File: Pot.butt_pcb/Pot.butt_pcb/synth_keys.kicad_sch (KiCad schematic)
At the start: 60 parts, among them SW11 Cherry_MX_1u, SW12 Cherry_MX_1u, SW13 Cherry_MX_1u, SW14 Cherry_MX_1u, SW15 Cherry_MX_1u, SW16 Cherry_MX_1u, SW17 Cherry_MX_1u, SW18 Cherry_MX_1u, SW19 Cherry_MX_1u, SW20 Cherry_MX_1u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

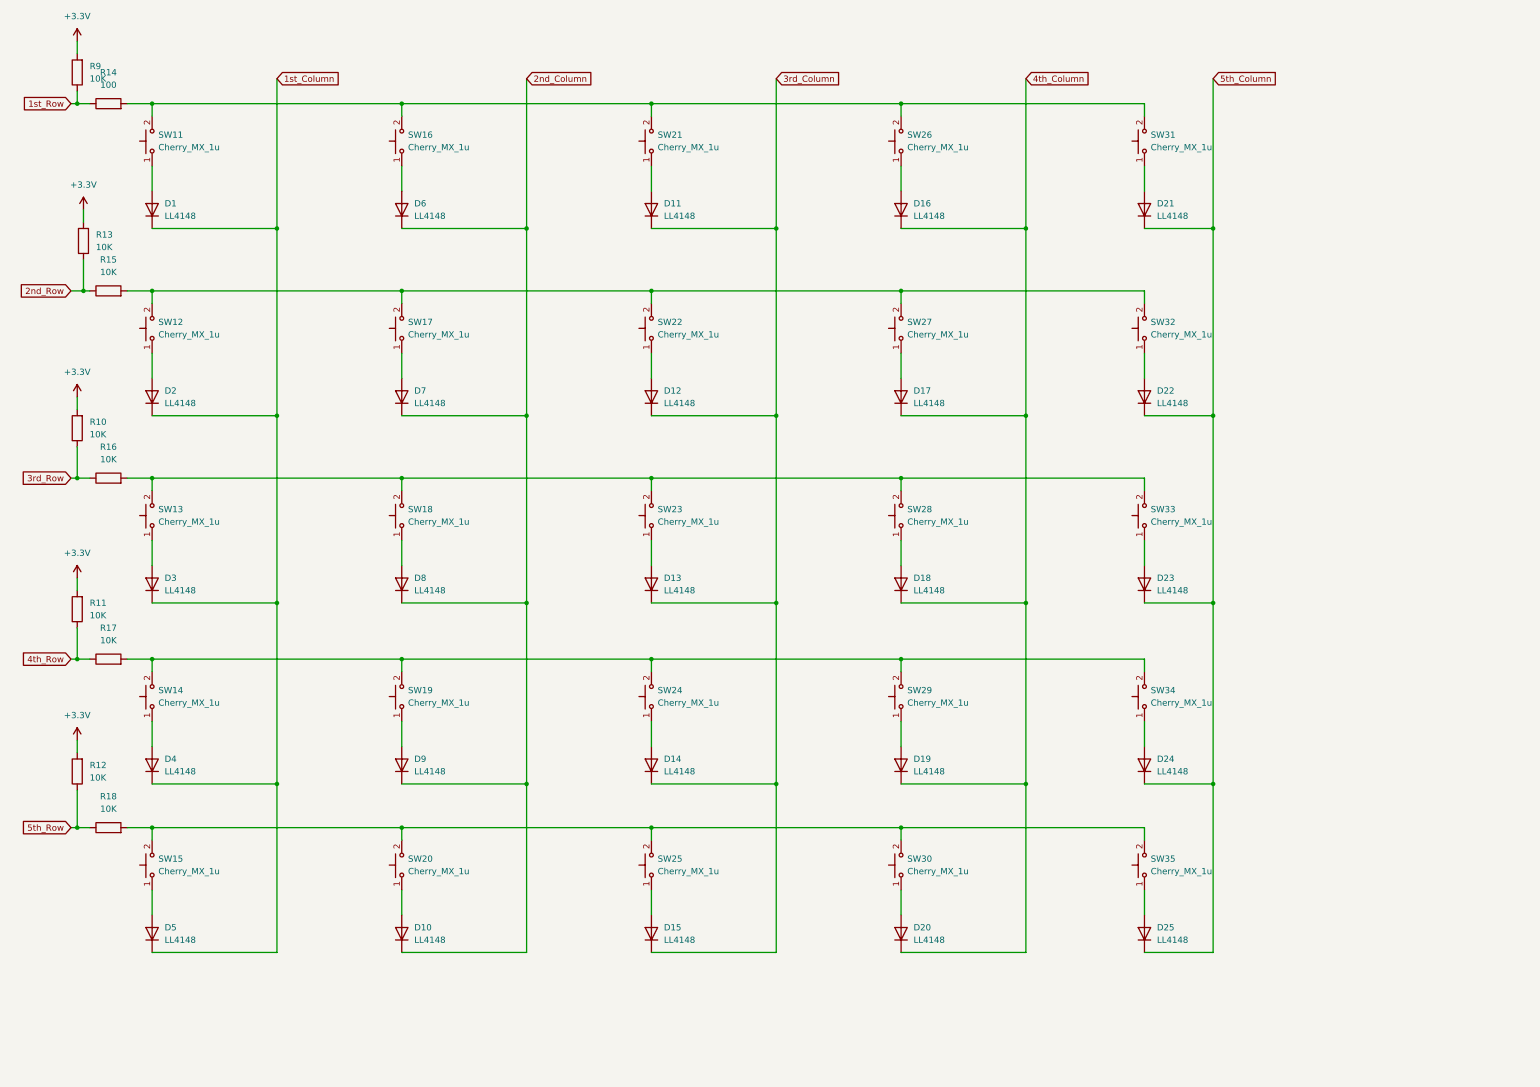
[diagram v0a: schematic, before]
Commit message: fixing keyboard and pot project schematics
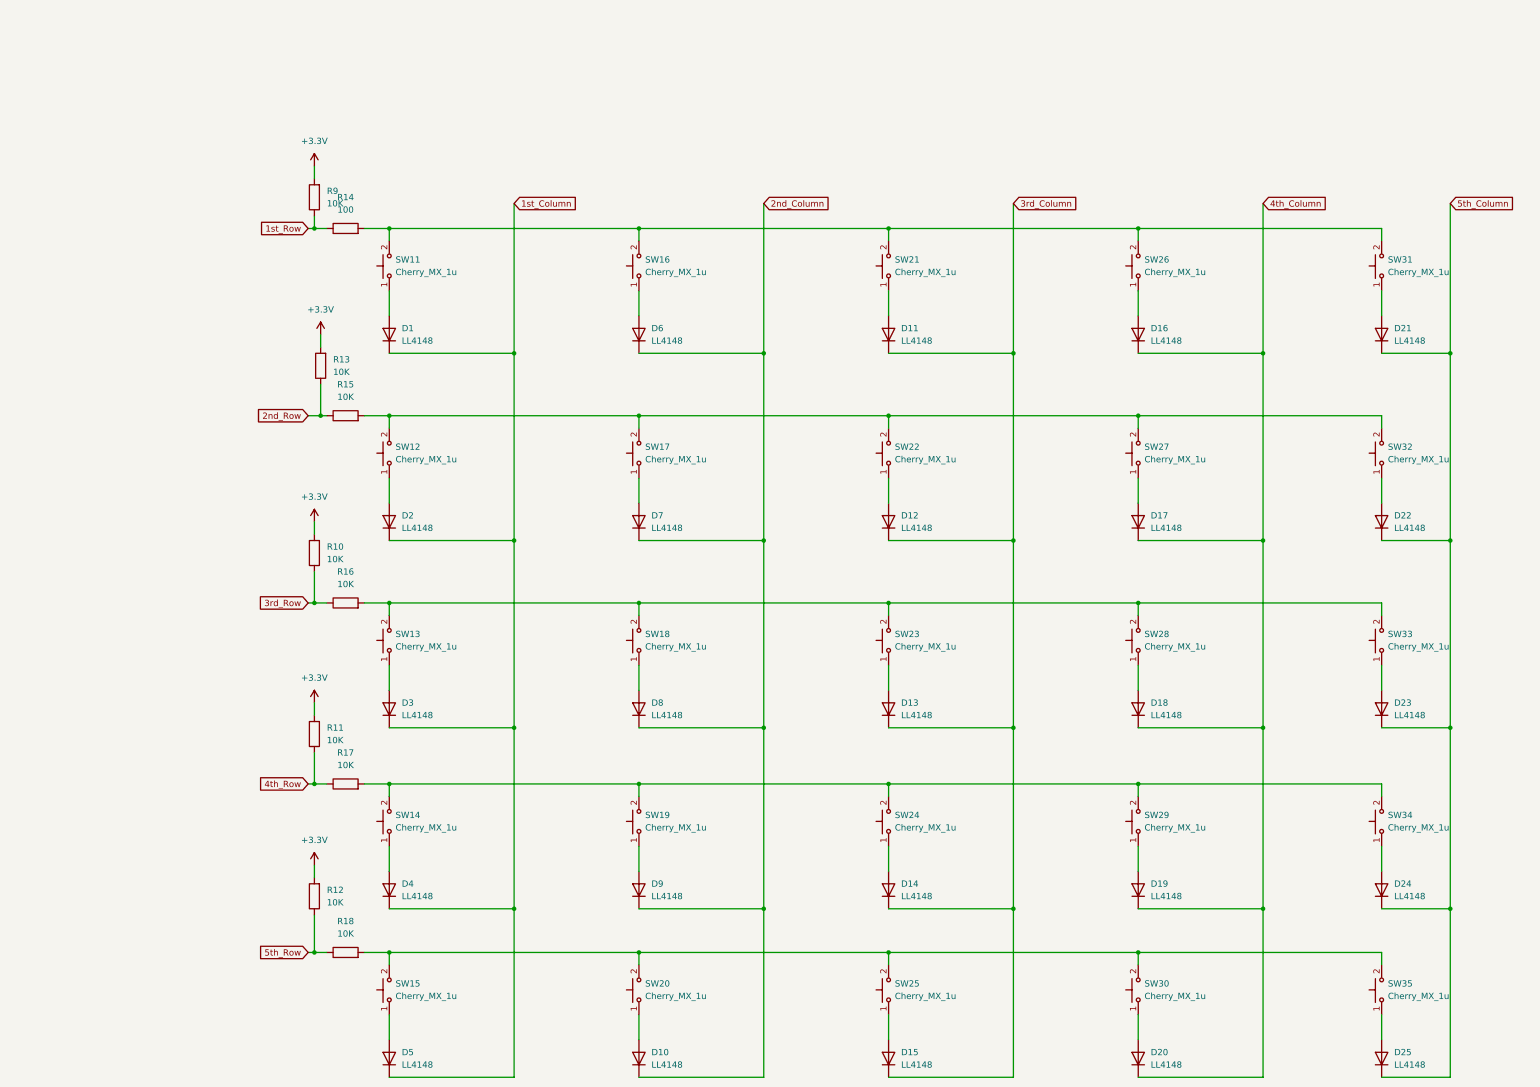
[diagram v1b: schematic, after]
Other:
- moved on the sheet: D1, D10, D11, D12, D13, D14, D15, D16, D17, D18, D19, D2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

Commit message: Pot.but_pcb in progress
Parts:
- R15, R16, R17, R18: value 10K -> 100
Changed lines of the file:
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@@
     (in_bom yes) (on_board yes) (fields_autoplaced)
     (property "Reference" "R17" (id 0) (at 85.09 154.94 90))
-    (property "Value" "10K" (id 1) (at 85.09 157.48 90))
+    (property "Value" "100" (id 1) (at 85.09 157.48 90))
     (property "Footprint" "Resistor_SMD:R_0805_2012Metric_Pad1.20x1.40mm_HandSolder" (id 2) (at 85.09 163.068 90)
       (effects (font (size 1.27 1.27)) hide)
@@
     (in_bom yes) (on_board yes) (fields_autoplaced)
     (property "Reference" "R18" (id 0) (at 85.09 189.23 90))
-    (property "Value" "10K" (id 1) (at 85.09 191.77 90))
+    (property "Value" "100" (id 1) (at 85.09 191.77 90))
     (property "Footprint" "Resistor_SMD:R_0805_2012Metric_Pad1.20x1.40mm_HandSolder" (id 2) (at 85.09 197.358 90)
       (effects (font (size 1.27 1.27)) hide)
@@
     (in_bom yes) (on_board yes) (fields_autoplaced)
     (property "Reference" "R16" (id 0) (at 85.09 118.11 90))
-    (property "Value" "10K" (id 1) (at 85.09 120.65 90))
+    (property "Value" "100" (id 1) (at 85.09 120.65 90))
     (property "Footprint" "Resistor_SMD:R_0805_2012Metric_Pad1.20x1.40mm_HandSolder" (id 2) (at 85.09 126.238 90)
       (effects (font (size 1.27 1.27)) hide)
@@
     (in_bom yes) (on_board yes) (fields_autoplaced)
     (property "Reference" "R15" (id 0) (at 85.09 80.01 90))
-    (property "Value" "10K" (id 1) (at 85.09 82.55 90))
+    (property "Value" "100" (id 1) (at 85.09 82.55 90))
     (property "Footprint" "Resistor_SMD:R_0805_2012Metric_Pad1.20x1.40mm_HandSolder" (id 2) (at 85.09 88.138 90)
       (effects (font (size 1.27 1.27)) hide)
